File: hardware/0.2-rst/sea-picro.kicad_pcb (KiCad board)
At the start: 4 copper layers, 17.8 x 33 mm, 54 parts, among them J1 USB_C_Receptacle_USB2.0, J2 0.1" x 12, J3 0.1" x 12, J4 D+, J5 D-, J6 0.1" x 5, Q1 2N7002VC-7, Q2 2N7002VC-7, U1 ME6211C33M5G-N, U2 GD25Q64CWIGR, U3 RP2040, Y1 12MHz

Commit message: split into rst and ext versionN
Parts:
- removed J6: 0.1" x 5, josh-connectors:PinHeader_1x05_P2.54mm_Circle
- added SW1: SWITCH, josh-buttons-switches:SW_Push_KMR2, F.Cu at (130.9, 104.6)
- added TP3: BOOT, TestPoint:TestPoint_Pad_D1.0mm, F.Cu at (123.7, 107.0)
- added TP4: CLK, josh-test-point:TestPoint_THTPad_D1.0mm_Drill0.5mm_NO_SILK, B.Cu at (121.8, 100.0)
- added TP5: IO, josh-test-point:TestPoint_THTPad_D1.0mm_Drill0.5mm_NO_SILK, B.Cu at (130.5, 100.5)
- TP1: value CLK -> nRST; footprint josh-test-point:TestPoint_THTPad_D1.0mm_Drill0.5mm_NO_SILK -> TestPoint:TestPoint_Pad_D1.0mm; moved to F.Cu
- TP2: value IO -> DELAY; footprint josh-test-point:TestPoint_THTPad_D1.0mm_Drill0.5mm_NO_SILK -> TestPoint:TestPoint_Pad_D1.0mm; moved to F.Cu
- moved TP2 11.4 mm to (121.2, 107.0), turned to 0 degrees
- moved TP1 8.29 mm to (126.2, 107.0), turned to 0 degrees
- moved Q2 4.63 mm to (126.7, 105.3)
- moved R12 4.52 mm to (131.8, 100.7), turned to 90 degrees
- moved R13 3.92 mm to (125.2, 103.7), turned to 180 degrees
- moved C19 3.92 mm to (120.7, 105.3)
- moved C6 3.75 mm to (120.7, 102.6)
- moved C5 3.64 mm to (122.1, 105.8), turned to 180 degrees
- moved Q1 3.42 mm to (127.7, 103.0)
- moved R11 3.29 mm to (124.4, 105.8)
- moved R15 2.60 mm to (129.2, 101.4), turned to 0 degrees
- moved R14 2.33 mm to (124.4, 104.9)
- moved R5 1.10 mm to (128.6, 105.0), turned to 90 degrees
- moved R9 0.78 mm to (124.7, 102.3)
- moved C8 0.74 mm to (125.7, 102.3)
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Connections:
- TP1 pad 1: /SWDCLK -> /nRST
- TP2 pad 1: /SWDIO -> Net-(C19-Pad1)
- U3 pad 13: /10 -> unconnected-(U3-Pad13)
- U3 pad 14: /11 -> unconnected-(U3-Pad14)
- U3 pad 15: /15 -> unconnected-(U3-Pad15)
- U3 pad 29: /18 -> unconnected-(U3-Pad29)
- U3 pad 30: /19 -> unconnected-(U3-Pad30)
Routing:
- net /15: track 13.2 -> 0.00 mm
- net /BOOT: track 1.23 -> 14.3 mm, vias 0 -> 2
- net /18: track 12.1 -> 0.00 mm
- net /11: track 11.1 -> 0.00 mm
- net /19: track 10.5 -> 0.00 mm
- net /10: track 10.2 -> 0.00 mm
- net /nRST: track 7.94 -> 17.8 mm, vias 2 -> 0
- net /SWITCH: track 23.9 -> 30.5 mm, vias 2 -> 4
- net Net-(Q1-Pad4): track 8.55 -> 5.69 mm
- net /FLASH_nCS: track 23.3 -> 22.1 mm
- net Net-(C6-Pad2): track 5.50 -> 6.62 mm
- net Net-(C7-Pad2): track 4.06 -> 3.24 mm
- net Net-(R9-Pad2): track 1.88 -> 2.65 mm
- net /7: track 8.62 -> 7.95 mm
- net Net-(C19-Pad1): track 8.04 -> 8.68 mm
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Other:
- board text added: "B"
- board text added: "R"
- board text removed: "10"
- board text removed: "11"
- board text removed: "15"
- board text removed: "18"
- board text removed: "19"

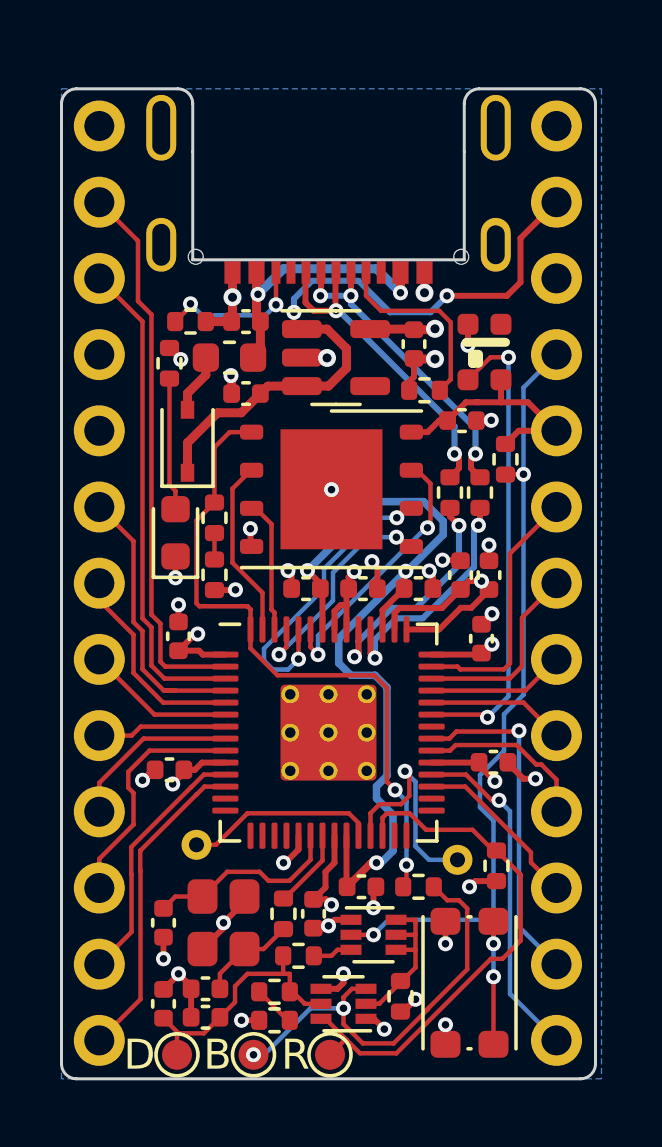
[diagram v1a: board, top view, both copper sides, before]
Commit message: add usb vbus detect
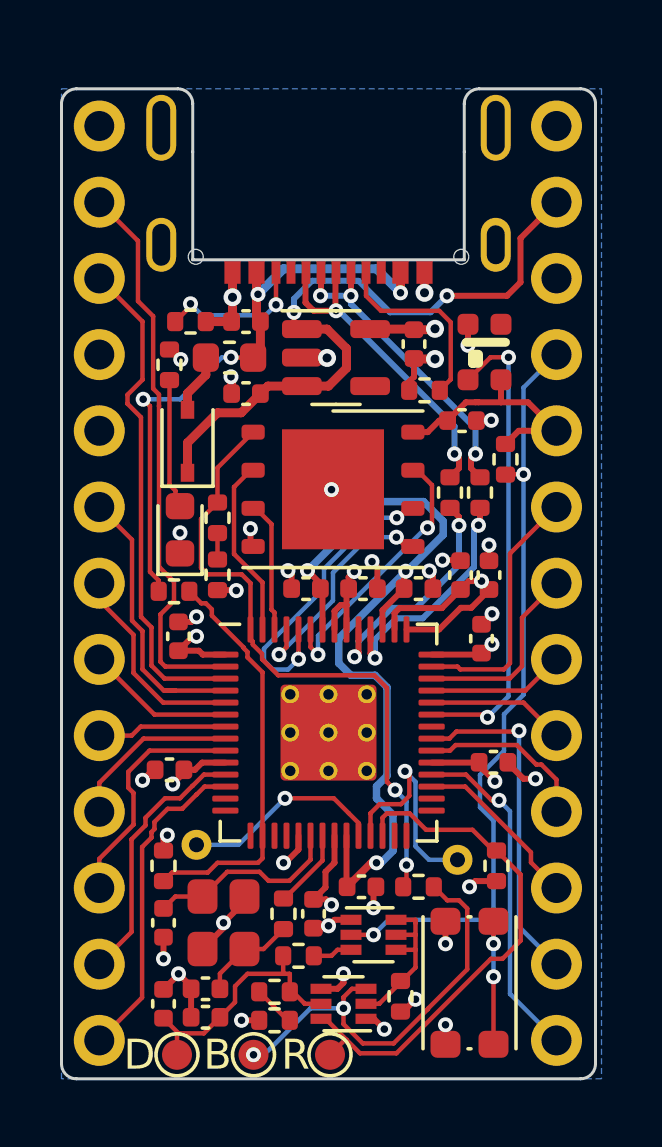
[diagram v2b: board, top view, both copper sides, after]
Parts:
- added R16: 2K2, Resistor_SMD:R_0402_1005Metric, F.Cu at (121.0, 91.5)
- added R17: 5K1, Resistor_SMD:R_0402_1005Metric, F.Cu at (120.7, 100.7)
- R3: value 1K -> 2K2
- moved D2 0.18 mm to (121.2, 89.5)
- moved R10 0.10 mm to (122.5, 89.1)
- moved R6 0.10 mm to (122.5, 91.0)
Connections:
- U3 pad 16: unconnected-(U3-Pad16) -> /VBUS_DETECT
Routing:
- net /VBUS_DETECT: track 0.00 -> 13.6 mm
- net VBUS: track 9.15 -> 20.0 mm, vias 2 -> 4
- net /FLASH_nCS: track 22.1 -> 21.3 mm
- net GND: track 27.9 -> 28.5 mm, vias 30 -> 31
- net /SWDCLK: track 6.39 -> 6.81 mm, vias 0 -> 1

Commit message: add LED driver and more test points
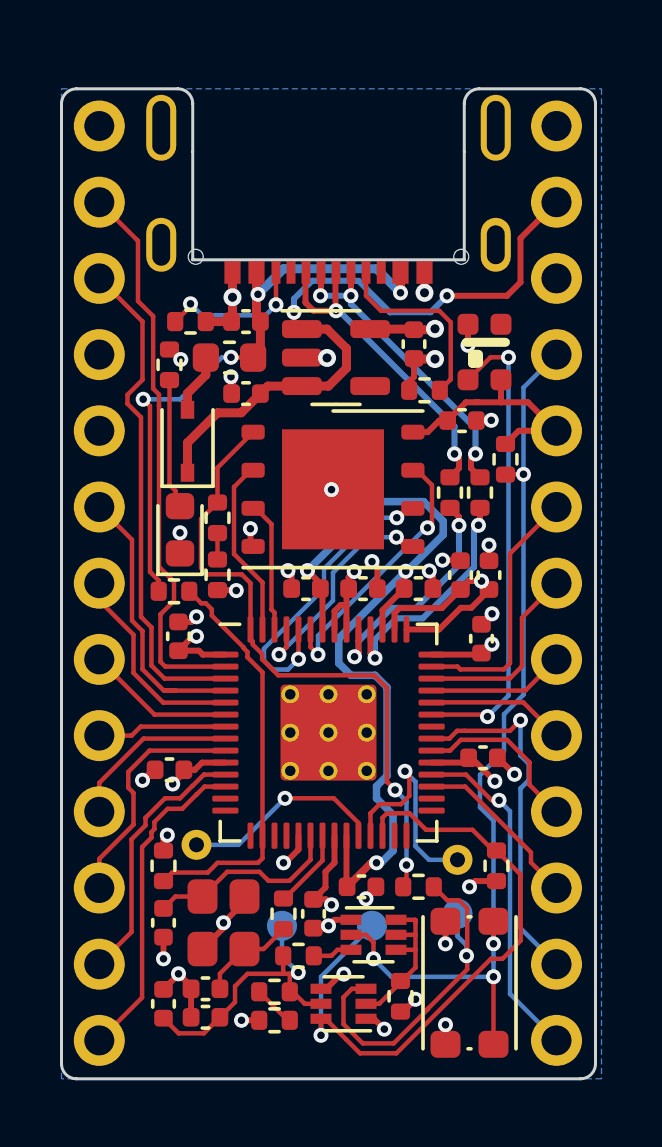
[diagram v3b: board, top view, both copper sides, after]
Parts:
- TP1, TP2, TP3: footprint TestPoint:TestPoint_Pad_D1.0mm -> josh-test-point:TestPoint_SMDPad_D1.0mm_NO_SILK; moved to B.Cu
- moved TP3 8.27 mm to (130.5, 102.3), turned to 180 degrees
- moved TP2 5.54 mm to (124.7, 102.7), turned to 180 degrees
- moved TP1 4.52 mm to (127.7, 102.7), turned to 180 degrees
- moved C14 0.38 mm to (131.3, 97.1)
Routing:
- net /nRST: track 17.8 -> 21.9 mm, vias 0 -> 1
- net /BOOT: track 14.3 -> 12.1 mm, vias 2 -> 1
- net Net-(C19-Pad1): track 8.68 -> 10.0 mm, vias 0 -> 1
- net /23_MOSI: track 11.3 -> 12.1 mm
- net GND: track 28.5 -> 27.8 mm
- net /SWITCH: track 30.5 -> 31.2 mm
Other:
- board text added: "DEL"

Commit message: update vscore markings
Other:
- board text added: "<- V score along these lines -> note USB connector sticks out 2mm"
- board text removed: "<- Vscore along -> these edges if panelising"
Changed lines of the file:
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@@
   (gr_line (start 119.75 77.25) (end 119.25 76.75) (layer "B.SilkS") (width 0.15))
   (gr_line (start 133.15 76.7) (end 132.95 76.9) (layer "B.SilkS") (width 0.15))
-  (gr_line (start 135.1 68.5) (end 135.1 114) (layer "Dwgs.User") (width 0.1))
-  (gr_line (start 117.3 68.5) (end 117.3 114) (layer "Dwgs.User") (width 0.1))
+  (gr_line (start 111.4 107.8) (end 135.4 107.8) (layer "Dwgs.User") (width 0.1))
+  (gr_line (start 111.4 74.8) (end 135.4 74.8) (layer "Dwgs.User") (width 0.1))
   (gr_line (start 117.3 75.3) (end 117.3 107.3) (layer "Edge.Cuts") (width 0.1))
   (gr_line (start 117.8 107.8) (end 134.6 107.8) (layer "Edge.Cuts") (width 0.1))
@@
     (effects (font (size 1 1) (thickness 0.15)) (justify mirror))
   )
-  (gr_text "<- Vscore along ->\nthese edges if\npanelising" (at 126.1 70.7) (layer "Dwgs.User")
+  (gr_text "<- V score along these lines ->\nnote USB connector sticks out 2mm" (at 113.6 91 90) (layer "Dwgs.User")
     (effects (font (size 1 1) (thickness 0.15)))
   )

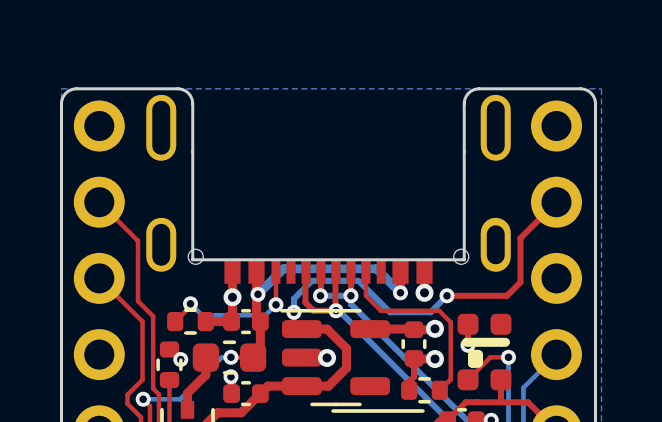
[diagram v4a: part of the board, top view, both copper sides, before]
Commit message: update ldo caps to 1u
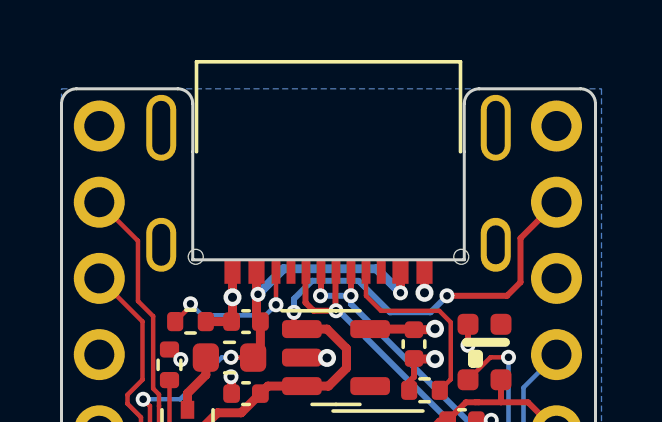
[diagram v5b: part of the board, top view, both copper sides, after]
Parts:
- C12, C9: value 2u2 -> 1u
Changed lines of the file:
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@@
     (fp_line (start -3 -1.5) (end -2 -2.5) (layer "F.Fab") (width 0.1))
     (fp_line (start -3 2.5) (end -3 -1.5) (layer "F.Fab") (width 0.1))
-    (pad "" smd roundrect (at -0.85 1) (size 1.37 1.61) (layers "F.Paste") (roundrect_rratio 0.182482))
-    (pad "" smd roundrect (at 0.85 1) (size 1.37 1.61) (layers "F.Paste") (roundrect_rratio 0.182482))
-    (pad "" smd roundrect (at 0.85 -1) (size 1.37 1.61) (layers "F.Paste") (roundrect_rratio 0.182482))
-    (pad "" smd roundrect (at -0.85 -1) (size 1.37 1.61) (layers "F.Paste") (roundrect_rratio 0.182482))
+    (pad "" smd roundrect (at -0.85 1) (size 1.37 1.61) (layers "F.Paste") (roundrect_rratio 0.1824817518))
+    (pad "" smd roundrect (at 0.85 1) (size 1.37 1.61) (layers "F.Paste") (roundrect_rratio 0.1824817518))
+    (pad "" smd roundrect (at 0.85 -1) (size 1.37 1.61) (layers "F.Paste") (roundrect_rratio 0.1824817518))
+    (pad "" smd roundrect (at -0.85 -1) (size 1.37 1.61) (layers "F.Paste") (roundrect_rratio 0.1824817518))
     (pad "1" smd roundrect (at -2.6625 -1.905) (size 0.775 0.5) (layers "F.Cu" "F.Paste" "F.Mask") (roundrect_rratio 0.25)
       (net 33 "/FLASH_nCS") (pinfunction "~{CS}") (pintype "input"))
@@
       (effects (font (size 0.75 0.75) (thickness 0.1)))
     )
+    (fp_line (start 4.4 3) (end 4.4 0) (layer "F.SilkS") (width 0.12))
+    (fp_line (start 4.4 0) (end -4.4 0) (layer "F.SilkS") (width 0.12))
+    (fp_line (start -4.4 0) (end -4.4 3) (layer "F.SilkS") (width 0.12))
+    (fp_line (start 4.525 3) (end 4.525 6.6) (layer "Edge.Cuts") (width 0.1))
     (fp_line (start -4.525 6.6) (end 4.525 6.6) (layer "Edge.Cuts") (width 0.1))
     (fp_line (start -4.525 3) (end -4.525 6.6) (layer "Edge.Cuts") (width 0.1))
-    (fp_line (start 4.525 3) (end 4.525 6.6) (layer "Edge.Cuts") (width 0.1))
-    (pad "" smd roundrect (at -5.825 6.1) (size 1.5 1.8) (layers "F.Paste") (roundrect_rratio 0.2))
+    (pad "" smd roundrect (at -5.825 2.2) (size 1.5 2.2) (layers "F.Paste") (roundrect_rratio 0.2))
     (pad "" smd roundrect (at 5.825 6.1) (size 1.5 1.8) (layers "F.Paste") (roundrect_rratio 0.2))
-    (pad "" smd roundrect (at 5.8 2.2) (size 1.5 2.2) (layers "F.Paste") (roundrect_rratio 0.2))
     (pad "" np_thru_hole circle (at -4.425 6.5) (size 0.5 0.5) (drill 0.5) (layers F&B.Cu *.Mask))
     (pad "" np_thru_hole circle (at 4.425 6.5) (size 0.5 0.5) (drill 0.5) (layers F&B.Cu *.Mask))
-    (pad "" smd roundrect (at -5.825 2.2) (size 1.5 2.2) (layers "F.Paste") (roundrect_rratio 0.2))
+    (pad "" smd roundrect (at 5.8 2.2) (size 1.5 2.2) (layers "F.Paste") (roundrect_rratio 0.2))
+    (pad "" smd roundrect (at -5.825 6.1) (size 1.5 1.8) (layers "F.Paste") (roundrect_rratio 0.2))
     (pad "A1" smd rect (at -3.2 7) (size 0.54 0.8) (layers "F.Cu" "F.Paste" "F.Mask")
       (net 1 "GND") (pinfunction "GND") (pintype "power_in") (clearance 0.15))
     (pad "A1" smd rect (at 3.2 7) (size 0.54 0.8) (layers "F.Cu" "F.Paste" "F.Mask")
       (net 1 "GND") (pinfunction "GND") (pintype "power_in") (clearance 0.15))
+    (pad "A4" smd rect (at -2.4 7) (size 0.54 0.8) (layers "F.Cu" "F.Paste" "F.Mask")
+      (net 5 "VBUS") (pinfunction "VBUS") (pintype "power_in") (clearance 0.15))
     (pad "A4" smd rect (at 2.4 7) (size 0.54 0.8) (layers "F.Cu" "F.Paste" "F.Mask")
-      (net 5 "VBUS") (pinfunction "VBUS") (pintype "power_in") (clearance 0.15))
-    (pad "A4" smd rect (at -2.4 7) (size 0.54 0.8) (layers "F.Cu" "F.Paste" "F.Mask")
       (net 5 "VBUS") (pinfunction "VBUS") (pintype "power_in") (clearance 0.15))
     (pad "A5" smd rect (at 1.25 7) (size 0.3 0.8) (layers "F.Cu" "F.Paste" "F.Mask")
@@
     (tags "capacitor")
     (property "JLC Basic" "Y")
-    (property "LCSC" "C12530")
-    (property "MPN " "CL05A225MQ5NSNC")
+    (property "LCSC" "C15849")
+    (property "MPN " "CL10A105KB8NNNC")
     (property "Manufacturer" "Samsung Electro-Mechanics")
     (property "Sheetfile" "sea-picro.kicad_sch")
@@
       (effects (font (size 1 1) (thickness 0.15)))
     )
-    (fp_text value "2u2" (at 0 1.16) (layer "F.Fab") hide
+    (fp_text value "1u" (at 0 1.16) (layer "F.Fab") hide
       (effects (font (size 1 1) (thickness 0.15)))
     )
@@
     (tags "capacitor")
     (property "JLC Basic" "Y")
-    (property "LCSC" "C12530")
-    (property "MPN " "CL05A225MQ5NSNC")
+    (property "LCSC" "C15849")
+    (property "MPN " "CL10A105KB8NNNC")
     (property "Manufacturer" "Samsung Electro-Mechanics")
     (property "Sheetfile" "sea-picro.kicad_sch")
@@
       (effects (font (size 1 1) (thickness 0.15)))
     )
-    (fp_text value "2u2" (at 0 1.16) (layer "F.Fab") hide
-      (effects (font (size 1 1) (thickness 0.15)))
-    )
+    (fp_text value "1u" (at 0 1.16) (layer "F.Fab") hide
+      (effects (font (size 1 1) (thickness 0.15)))
+    )

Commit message: fixes after assembly
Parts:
- U1: value ME6211C33M5G-N -> AP7365-33WG-7
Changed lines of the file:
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@@
     (tags "SOT TO_SOT_SMD")
     (property "JLC Basic" "N")
-    (property "LCSC" "C82942")
-    (property "MPN " "ME6211C33M5G-N")
-    (property "Manufacturer" "MICRONE(Nanjing Micro One Elec)")
+    (property "LCSC" "C150742")
+    (property "MPN " "AP7365-33WG-7 ")
+    (property "Manufacturer" "Diodes Incorporated")
     (property "Sheetfile" "sea-picro.kicad_sch")
     (property "Sheetname" "")
@@
       (effects (font (size 1 1) (thickness 0.15)))
     )
-    (fp_text value "ME6211C33M5G-N" (at 0 2.4) (layer "F.Fab") hide
+    (fp_text value "AP7365-33WG-7 " (at 0 2.4) (layer "F.Fab") hide
       (effects (font (size 1 1) (thickness 0.15)))
     )

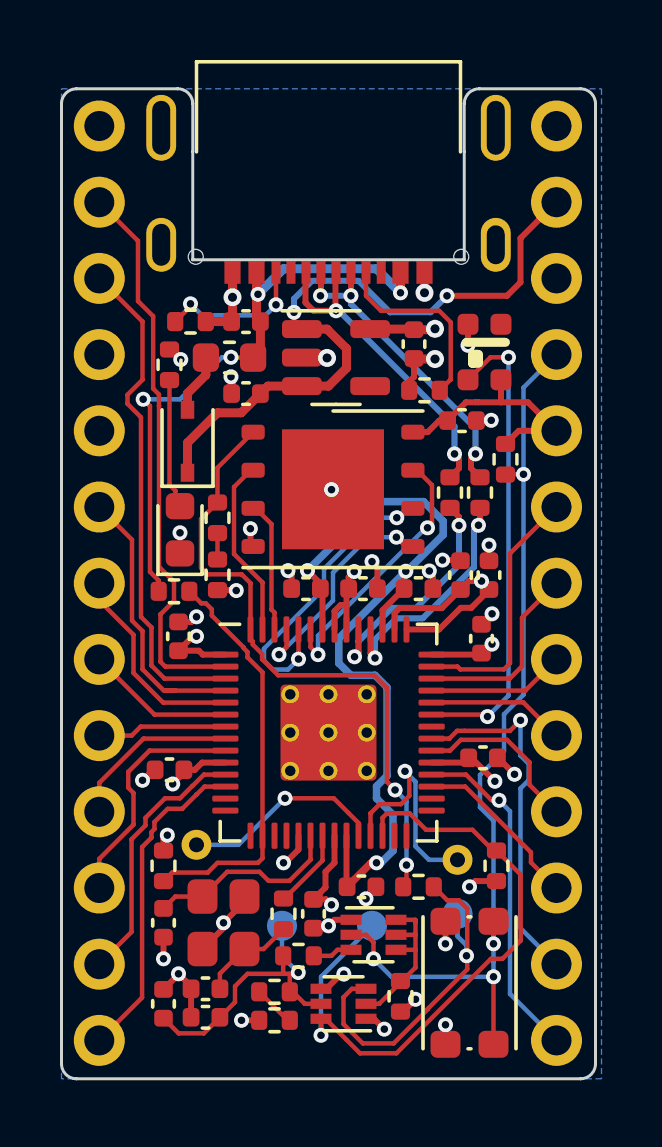
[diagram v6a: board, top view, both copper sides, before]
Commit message: Move R4 away from R8 in RST
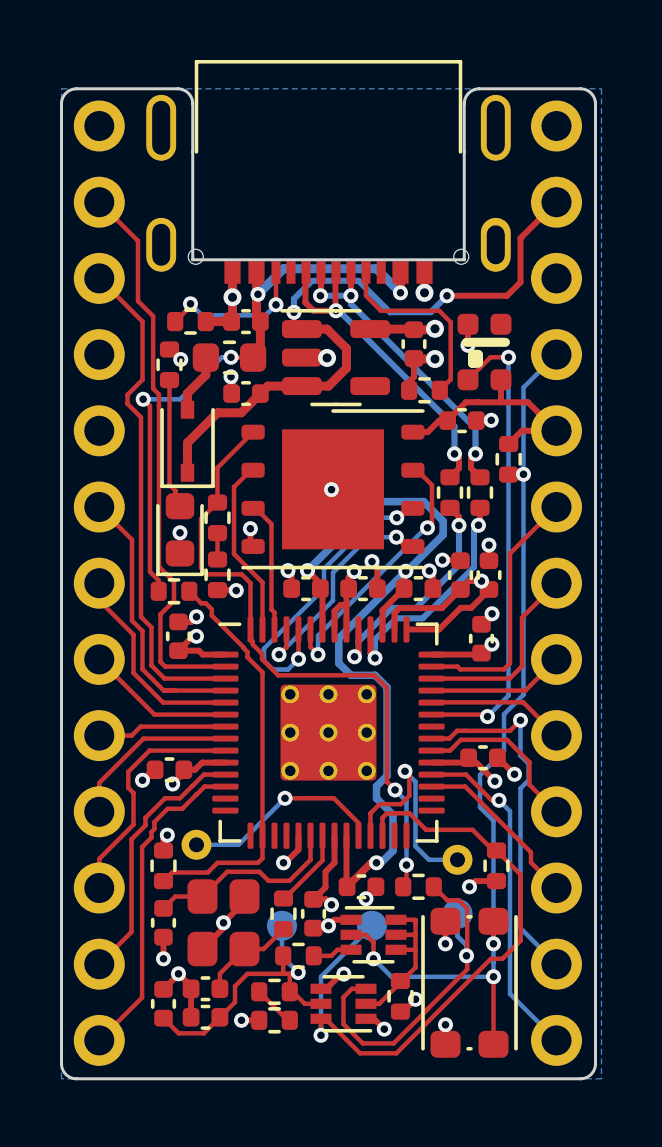
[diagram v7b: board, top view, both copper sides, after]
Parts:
- moved R4 0.11 mm to (132.2, 87.2)
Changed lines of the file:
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@@
   )
   (footprint "Resistor_SMD:R_0402_1005Metric" (layer "F.Cu")
-    (at 132.1 87.15 -90)
+    (at 132.207 87.15 -90)
     (descr "Resistor SMD 0402 (1005 Metric), square (rectangular) end terminal, IPC_7351 nominal, (Body size source: IPC-SM-782 page 72, https://www.pcb-3d.com/wordpress/wp-content/uploads/ipc-sm-782a_amendment_1_and_2.pdf), generated with kicad-footprint-generator")
     (tags "resistor")
@@
   (segment (start 130.6 91.49) (end 130.88 91.21) (width 0.2) (layer "F.Cu") (net 7))
   (segment (start 121.2 93.53) (end 121.68 93.05) (width 0.2) (layer "F.Cu") (net 7))
-  (segment (start 132.54 86.2) (end 132.1 86.64) (width 0.2) (layer "F.Cu") (net 7))
   (segment (start 131.09 101.21) (end 130.9 101.4) (width 0.2) (layer "F.Cu") (net 7))
   (segment (start 121.38 97.599146) (end 121.006859 97.972287) (width 0.2) (layer "F.Cu") (net 7))
@@
   (segment (start 131.95 84.5) (end 131.95 85.25) (width 0.2) (layer "F.Cu") (net 7))
   (segment (start 131.25 93.66) (end 131.3 93.61) (width 0.2) (layer "F.Cu") (net 7))
-  (segment (start 133.8 86.2) (end 132.54 86.2) (width 0.2) (layer "F.Cu") (net 7))
   (segment (start 129.05 82.83) (end 129.72 82.83) (width 0.3) (layer "F.Cu") (net 7))
   (segment (start 131.55 91.51) (end 131.55 91.49) (width 0.2) (layer "F.Cu") (net 7))
   (segment (start 129.89 85.86) (end 129.505 86.245) (width 0.2) (layer "F.Cu") (net 7))
+  (segment (start 132.647 86.2) (end 132.207 86.64) (width 0.2) (layer "F.Cu") (net 7))
   (segment (start 122.4 91.51) (end 123.110501 91.51) (width 0.2) (layer "F.Cu") (net 7))
   (segment (start 126.12 101.82) (end 126.3 102) (width 0.2) (layer "F.Cu") (net 7))
@@
   (segment (start 125.7 101.82) (end 126.12 101.82) (width 0.2) (layer "F.Cu") (net 7))
   (segment (start 128.64 105.61) (end 129.1 105.15) (width 0.2) (layer "F.Cu") (net 7))
+  (segment (start 133.8 86.2) (end 132.647 86.2) (width 0.2) (layer "F.Cu") (net 7))
   (segment (start 126.4 100.6) (end 126.1 100.9) (width 0.2) (layer "F.Cu") (net 7))
   (via (at 126.3 102) (size 0.5) (drill 0.25) (layers "F.Cu" "B.Cu") (net 7))
@@
   (segment (start 127.75 93.16) (end 127.75 93.7755) (width 0.2) (layer "B.Cu") (net 46))
   (segment (start 131.7 106.45) (end 131.7 104.4) (width 0.15) (layer "F.Cu") (net 47))
-  (segment (start 132.11 87.65) (end 132.7 87.65) (width 0.15) (layer "F.Cu") (net 47))
+  (segment (start 132.207 87.66) (end 132.217 87.65) (width 0.15) (layer "F.Cu") (net 47))
   (segment (start 131.7 102.35) (end 131.7 103.3) (width 0.15) (layer "F.Cu") (net 47))
+  (segment (start 132.217 87.65) (end 132.7 87.65) (width 0.15) (layer "F.Cu") (net 47))
   (segment (start 127.45 103) (end 127.7 103.25) (width 0.15) (layer "F.Cu") (net 47))
   (segment (start 126.95 103) (end 127.45 103) (width 0.15) (layer "F.Cu") (net 47))
-  (segment (start 132.1 87.66) (end 132.11 87.65) (width 0.15) (layer "F.Cu") (net 47))
   (segment (start 127.7 103.25) (end 127.7 103.8) (width 0.15) (layer "F.Cu") (net 47))
   (via (at 131.7 104.4) (size 0.5) (drill 0.25) (layers "F.Cu" "B.Cu") (net 47))
